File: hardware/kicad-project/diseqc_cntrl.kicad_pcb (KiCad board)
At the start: 4 copper layers, 90 x 100 mm, 142 parts, among them IC1 TPS560200DBVR, IC2 STM32F407VGT6, IC3 FM24CL16B-GTR, IC4 USBLC6-2P6, IC5 LNBH26PQR, IC6 IC_ETH_PHY_LAN8742A, J1 Barrel Jack, J2 Conn_01x04_Pin, J3 USB4110-GF-A, J4 TC2050, J5 USB4110-GF-A, J6 SMA_Sock, J7 SMA_Sock, J8 J_RJ45_SKT_MAG_LED, J9 Conn_01x04_Pin, SW1 Reset, U1 FT230XS, Y1 8MHZ, Y2 25MHZ

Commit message: Bugfix: IC6 pin 6 incorrectly connected to 3v3
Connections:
- C32 pad 1: +3.3VP -> Net-(IC6-VDDCR)
- C33 pad 1: +3.3VP -> Net-(IC6-VDDCR)
- IC6 pad 6: +3.3VP -> Net-(IC6-VDDCR)
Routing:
- net +3.3VP: track 42.5 -> 35.7 mm, vias 5 -> 4
- net Net-(IC6-VDDCR): track 0.00 -> 6.76 mm
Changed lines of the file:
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@@
 			(layers "F.Cu" "F.Mask" "F.Paste")
 			(roundrect_rratio 0.25)
-			(net "+3.3VP")
+			(net "Net-(IC6-VDDCR)")
 			(pinfunction "VDDCR_6")
 			(pintype "passive")
@@
 			(layers "F.Cu" "F.Mask" "F.Paste")
 			(roundrect_rratio 0.25)
-			(net "+3.3VP")
+			(net "Net-(IC6-VDDCR)")
 			(pintype "passive")
 		)
@@
 			(layers "F.Cu" "F.Mask" "F.Paste")
 			(roundrect_rratio 0.25)
-			(net "+3.3VP")
+			(net "Net-(IC6-VDDCR)")
 			(pintype "passive")
 		)
@@
 	)
 	(segment
-		(start 88.9 113.9)
-		(end 88 113.9)
-		(width 0.2)
-		(layer "F.Cu")
-		(net "+3.3VP")
-	)
-	(segment
 		(start 97.9125 114.2)
 		(end 97.9125 114.8875)
@@
 	)
 	(segment
-		(start 87.3 111.9375)
-		(end 87.32 111.9175)
-		(width 0.2)
-		(layer "F.Cu")
-		(net "+3.3VP")
-	)
-	(segment
 		(start 91.325 103.075)
 		(end 91.325 104.2)
@@
 	)
 	(segment
-		(start 88 113.9)
-		(end 87.32 113.22)
-		(width 0.2)
-		(layer "F.Cu")
-		(net "+3.3VP")
-	)
-	(segment
 		(start 85.98125 98.2625)
 		(end 88.9875 98.2625)
@@
 	)
 	(segment
-		(start 86.27 110.8675)
-		(end 87.32 111.9175)
-		(width 0.2)
-		(layer "F.Cu")
-		(net "+3.3VP")
-	)
-	(segment
 		(start 87.67 109.13)
 		(end 88.3 108.5)
@@
 	)
 	(segment
-		(start 87.32 113.22)
-		(end 87.32 111.9175)
-		(width 0.2)
-		(layer "F.Cu")
-		(net "+3.3VP")
-	)
-	(segment
 		(start 97.3 106.3)
 		(end 97.9125 106.9125)
@@
 	)
 	(segment
-		(start 85.97 110.8675)
-		(end 86.27 110.8675)
-		(width 0.2)
-		(layer "F.Cu")
-		(net "+3.3VP")
-	)
-	(segment
-		(start 88.9375 115.7)
-		(end 88.9375 113.9375)
-		(width 0.2)
-		(layer "F.Cu")
-		(net "+3.3VP")
-	)
-	(segment
 		(start 88.3 108.5)
 		(end 88.3375 108.5)
@@
 	)
 	(segment
-		(start 88.9375 113.9375)
-		(end 88.9 113.9)
-		(width 0.2)
-		(layer "F.Cu")
-		(net "+3.3VP")
-	)
-	(segment
 		(start 88.9875 98.2625)
 		(end 91.3 100.575)
@@
 	)
 	(via
-		(at 87.32 111.9175)
-		(size 0.8)
-		(drill 0.35)
-		(layers "F.Cu" "B.Cu")
-		(free yes)
-		(net "+3.3VP")
-	)
-	(via
 		(at 97.3 106.3)
 		(size 0.8)
@@
 		(net "/MCU/RXD1")
 	)
+	(segment
+		(start 88.9 113.9)
+		(end 88 113.9)
+		(width 0.2)
+		(layer "F.Cu")
+		(net "Net-(IC6-VDDCR)")
+	)
+	(segment
+		(start 88 113.9)
+		(end 87.32 113.22)
+		(width 0.2)
+		(layer "F.Cu")
+		(net "Net-(IC6-VDDCR)")
+	)
+	(segment
+		(start 86.27 110.8675)
+		(end 87.32 111.9175)
+		(width 0.2)
+		(layer "F.Cu")
+		(net "Net-(IC6-VDDCR)")
+	)
+	(segment
+		(start 87.32 113.22)
+		(end 87.32 111.9175)
+		(width 0.2)
+		(layer "F.Cu")
+		(net "Net-(IC6-VDDCR)")
+	)
+	(segment
+		(start 85.97 110.8675)
+		(end 86.27 110.8675)
+		(width 0.2)
+		(layer "F.Cu")
+		(net "Net-(IC6-VDDCR)")
+	)
+	(segment
+		(start 88.9375 115.7)
+		(end 88.9375 113.9375)
+		(width 0.2)
+		(layer "F.Cu")
+		(net "Net-(IC6-VDDCR)")
+	)
+	(segment
+		(start 88.9375 113.9375)
+		(end 88.9 113.9)
+		(width 0.2)
+		(layer "F.Cu")
+		(net "Net-(IC6-VDDCR)")
+	)
 	(zone

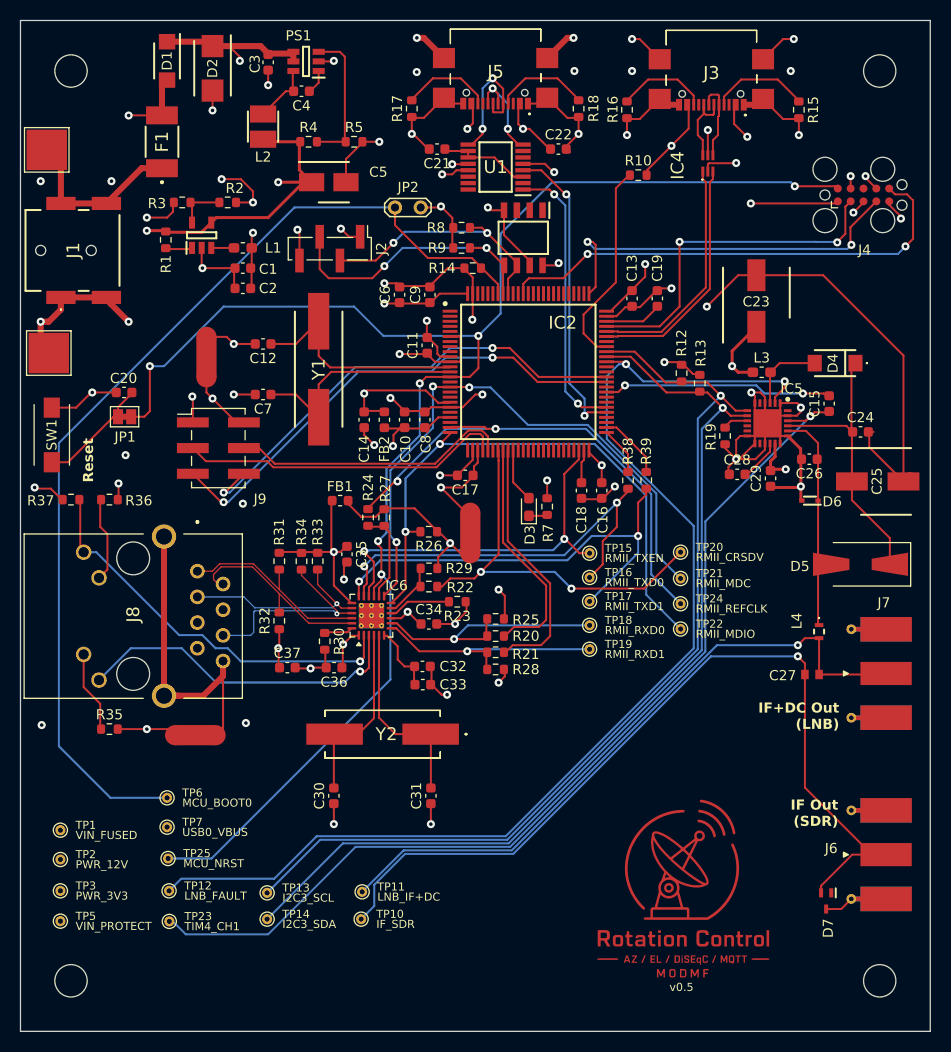
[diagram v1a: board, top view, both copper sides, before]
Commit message: Update power supply ICs
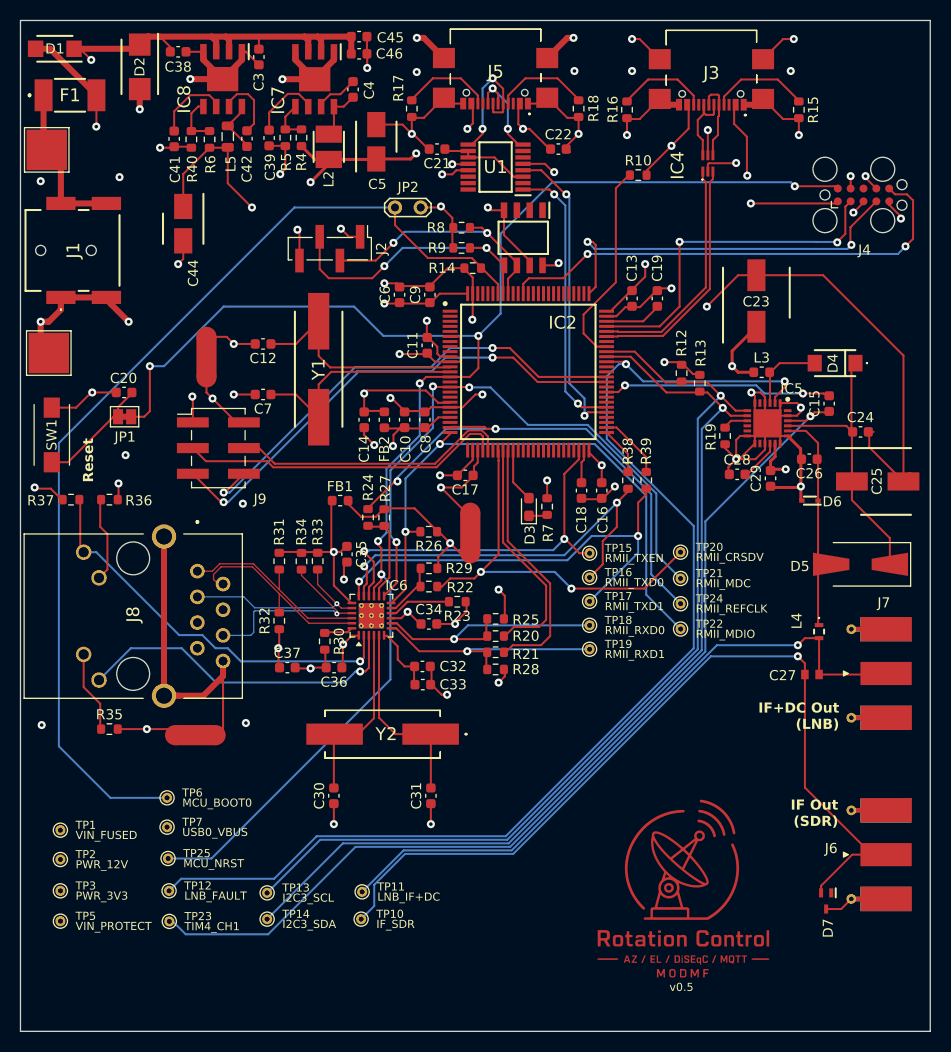
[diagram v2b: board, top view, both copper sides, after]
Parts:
- removed C1, C2: 10u, Capacitor_SMD:C_0603_1608Metric
- removed IC1: TPS560200DBVR, diseqc_cntrl:SOT95P280X145-5N
- removed L1: 10u, Inductor_SMD:L_0603_1608Metric_Pad1.05x0.95mm_HandSolder
- removed MOUNT01, MOUNT02, MOUNT03, MOUNT04: MountingHole_3.2mm_M3, diseqc_cntrl:MountingHole_3.2mm_M3
- removed PS1: TPS560430XDBVR, diseqc_cntrl:SOT95P280X145-6N
- removed R1: 100k, Resistor_SMD:R_0603_1608Metric
- removed R2: 61k9 1%, Resistor_SMD:R_0603_1608Metric
- removed R3: 20k 1%, Resistor_SMD:R_0603_1608Metric
- added C38: 4u7, Capacitor_SMD:C_0603_1608Metric, F.Cu at (65.6, 53.1)
- added C39: 1uF, Capacitor_SMD:C_0603_1608Metric, F.Cu at (74.6, 61.6)
- added C41: 1uF, Capacitor_SMD:C_0603_1608Metric, F.Cu at (65.2, 61.7)
- added C42: 100nF, Capacitor_SMD:C_0603_1608Metric, F.Cu at (72.4, 61.7)
- added C44: 10u 25V, diseqc_cntrl:CAPAE400X550N, F.Cu at (66.1, 70.1)
- added C45: 2u2, Capacitor_SMD:C_0603_1608Metric, F.Cu at (83.5, 51.6)
- added C46: 4u7, Capacitor_SMD:C_0603_1608Metric, F.Cu at (83.5, 53.3)
- added IC7: LMR36520ADDAR, ebnx_footprints:SOIC127P600X170-9N, F.Cu at (79.1, 55.8)
- added IC8: LMR36520ADDAR, ebnx_footprints:SOIC127P600X170-9N, F.Cu at (70.0, 55.8)
- added L5: 6u8, Inductor_SMD:L_0805_2012Metric, F.Cu at (70.5, 61.5)
- added R40: 43k2_1%, Resistor_SMD:R_0603_1608Metric, F.Cu at (66.9, 61.8)
- added R6: 100k 1%, Resistor_SMD:R_0603_1608Metric, F.Cu at (68.7, 61.8)
- L2: footprint diseqc_cntrl:INDPM3030X150N -> ebnx_footprints:INDPM3030X150N
- L3: footprint Inductor_SMD:L_0603_1608Metric_Pad1.05x0.95mm_HandSolder -> Inductor_SMD:L_0603_1608Metric
- R4: value 243k 1% -> 100k 1%
- R5: value 22k1 1% -> 9k09 1%
- moved D1 11.2 mm to (53.4, 52.8), turned to 180 degrees
- moved F1 10.2 mm to (54.9, 57.4), turned to 0 degrees
- moved D2 7.20 mm to (61.8, 54.6)
- moved R5 6.81 mm to (76.2, 61.6), turned to -90 degrees
- moved L2 6.80 mm to (80.5, 62.5)
- moved C5 6.17 mm to (85.2, 62.0), turned to 90 degrees
- moved C4 5.10 mm to (82.9, 56.8), turned to -90 degrees
- moved C3 1.05 mm to (73.6, 53.6)
- moved R4 0.81 mm to (77.8, 61.6), turned to 90 degrees
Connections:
- net Net-(PS1-FB) renamed /12V_FB
- net Net-(PS1-SW) renamed /12V_SW
- net VIN_FUSED renamed /VIN_FUSED
- net VIN_PROTECTED renamed /VIN_PROTECTED
- net VIN_RAW renamed /VIN_RAW
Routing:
- net +12V: track 212.3 -> 186.1 mm
- net GND: track 249.2 -> 270.7 mm, vias 49 -> 50
- net /VIN_PROTECTED: track 111.1 -> 130.0 mm
- net /12V_FB: track 13.9 -> 4.27 mm
- net Net-(IC8-VCC): track 0.00 -> 7.49 mm
- net Net-(IC7-VCC): track 0.00 -> 7.09 mm
- net Net-(IC8-BOOT): track 0.00 -> 6.81 mm
- net /3V3_SW: track 0.00 -> 5.32 mm
- net /3V3_FB: track 0.00 -> 5.02 mm
- net /3V3_VSENSE: track 4.70 -> 0.00 mm
- net +3V3: track 178.4 -> 183.0 mm, vias 14 -> 12
- net Net-(IC1-EN): track 2.65 -> 0.00 mm
- net Net-(IC1-PH): track 2.25 -> 0.00 mm
- net /VIN_FUSED: track 83.8 -> 86.0 mm
- net Net-(IC7-BOOT): track 2.35 -> 4.37 mm
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
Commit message: Re-added mounting holes.
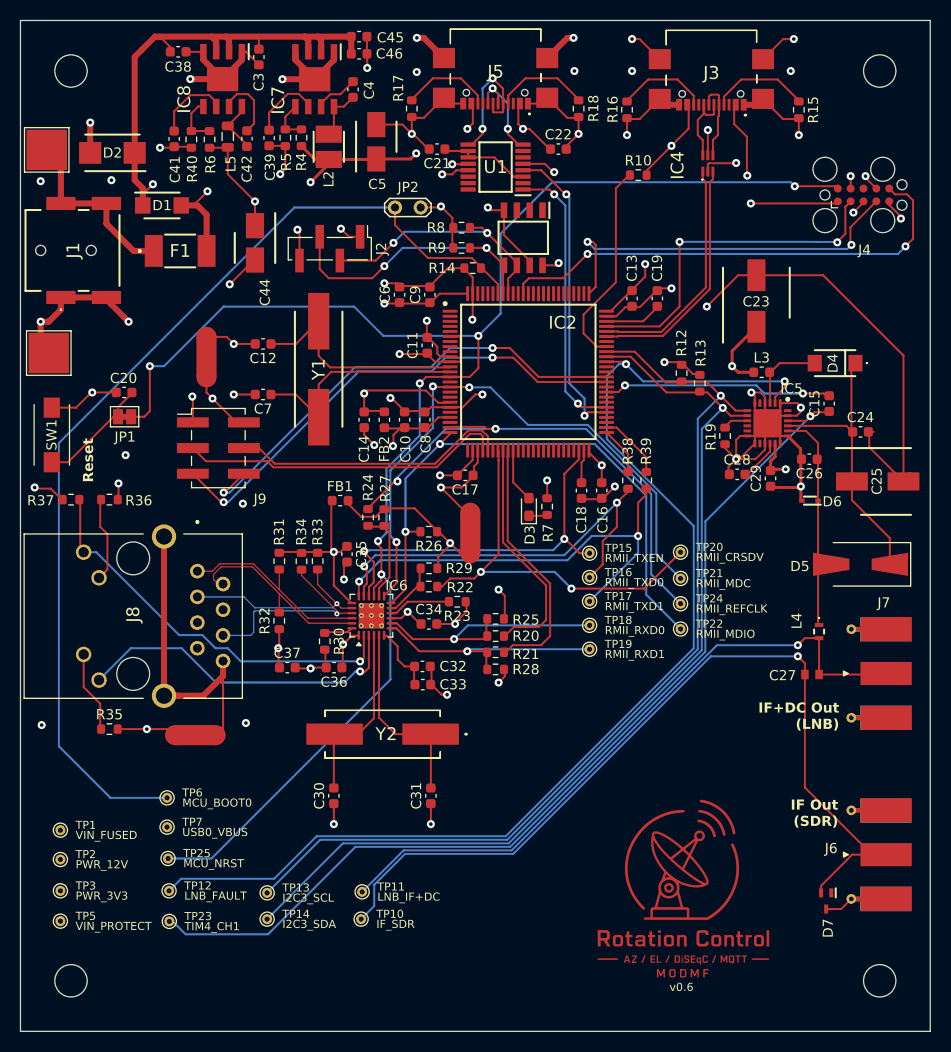
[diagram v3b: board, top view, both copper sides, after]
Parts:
- added MOUNT01: MountingHole_3.2mm_M3, diseqc_cntrl:MountingHole_3.2mm_M3, F.Cu at (55.0, 55.0)
- added MOUNT02: MountingHole_3.2mm_M3, diseqc_cntrl:MountingHole_3.2mm_M3, F.Cu at (135.0, 55.0)
- added MOUNT03: MountingHole_3.2mm_M3, diseqc_cntrl:MountingHole_3.2mm_M3, F.Cu at (55.0, 145.0)
- added MOUNT04: MountingHole_3.2mm_M3, diseqc_cntrl:MountingHole_3.2mm_M3, F.Cu at (135.0, 145.0)
- moved F1 18.9 mm to (65.8, 72.8)
- moved D1 18.8 mm to (64.0, 68.3), turned to 0 degrees
- moved D2 8.93 mm to (59.1, 63.1), turned to 180 degrees
- moved C44 7.35 mm to (73.2, 72.0)
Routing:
- net /VIN_FUSED: track 86.0 -> 79.3 mm
- net +3V3: track 183.0 -> 178.8 mm
- net /VIN_RAW: track 16.2 -> 18.9 mm
- net GND: track 270.7 -> 272.7 mm
- net /VIN_PROTECTED: track 130.0 -> 128.8 mm
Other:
- board text added: "v0.6"
- board text removed: "v0.5"

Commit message: Renumbered/annotated
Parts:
- renumbered C3 to C1, C5 to C11, C44 to C12, C6 to C13, C8 to C14, C7 to C15, C9 to C16, C10 to C17, C11 to C18, C12 to C19, C45 to C2, C13 to C20, C14 to C21, C16 to C22, C17 to C23, C18 to C24, C19 to C25, C20 to C26, C15 to C27, C21 to C28, C22 to C29, C38 to C3, C23 to C30, C24 to C31, C25 to C32, C26 to C33, C28 to C34, C29 to C35, C27 to C36, C30 to C37, C31 to C38, C32 to C39, C46 to C4, C33 to C40, C34 to C41, C35 to C42, C36 to C43, C37 to C44, C39 to C5, C41 to C6, C4 to C7, C42 to C8, FB2 to FB1, FB1 to FB2, IC7 to IC1, IC8 to IC2, IC2 to IC3, IC3 to IC4, IC4 to IC5, IC5 to IC6, IC6 to IC7, J9 to J2, J2 to J3, J3 to J4, J4 to J5, J5 to J6, J6 to J7, J7 to J8, J8 to J9, L2 to L1, L5 to L2, NT4 to NT2, R4 to R1, R12 to R10, R13 to R11, R14 to R12, R15 to R13, R16 to R14, R17 to R15, R18 to R16, R19 to R17, R38 to R18, R39 to R19, R5 to R2, R6 to R3, R40 to R4, R7 to R5, R8 to R6, R9 to R7, R10 to R8, TP26 to TP1, TP23 to TP15, TP15 to TP16, TP20 to TP17, TP21 to TP18, TP22 to TP19, TP27 to TP2, TP24 to TP20, TP16 to TP21, TP17 to TP22, TP18 to TP23, TP19 to TP24, TP1 to TP3, TP2 to TP4, TP3 to TP5, TP5 to TP6, TP25 to TP8, TP6 to TP9

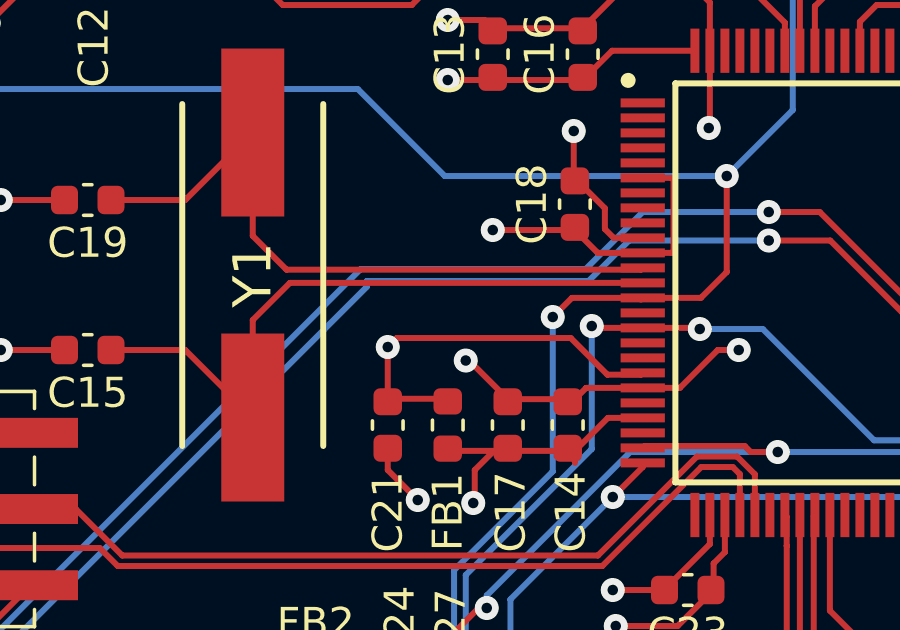
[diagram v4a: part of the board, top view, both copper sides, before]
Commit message: Replaced 10k pull-up on NRST
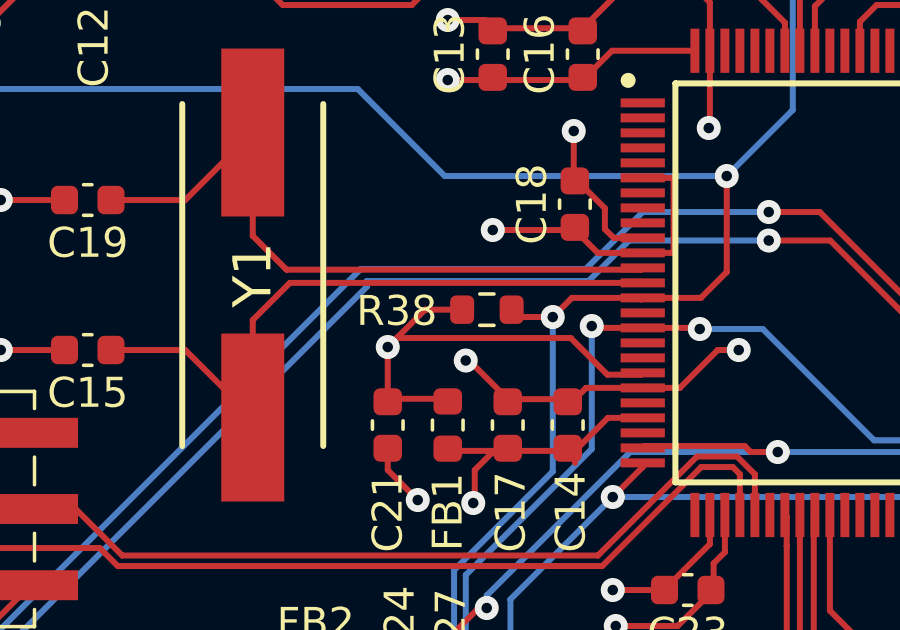
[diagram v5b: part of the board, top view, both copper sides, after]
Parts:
- added R38: 10k, Resistor_SMD:R_0603_1608Metric, F.Cu at (87.3, 85.7)
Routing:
- net +3V3: track 178.8 -> 181.8 mm
- net /MCU/NRST: track 162.5 -> 164.0 mm

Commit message: Decreased VBUS_SENSE (R8) to 1k
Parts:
- R1, R17, R18, R19, R2, R20, R21, R22, R23, R24, R25, R26, R27, R28, R29, R3, R30, R31, R32, R33, R34, R38, R4: footprint Resistor_SMD:R_0603_1608Metric -> Resistor_SMD:R_0603_1608Metric_Pad0.98x0.95mm_HandSolder
